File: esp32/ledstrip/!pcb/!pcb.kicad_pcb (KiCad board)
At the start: 2 copper layers, 100 x 100 mm, 11 parts, among them J1 Barrel_Jack_Switch, J2 Conn_01x03, U1 ESP32 MINI, U2 INMP441

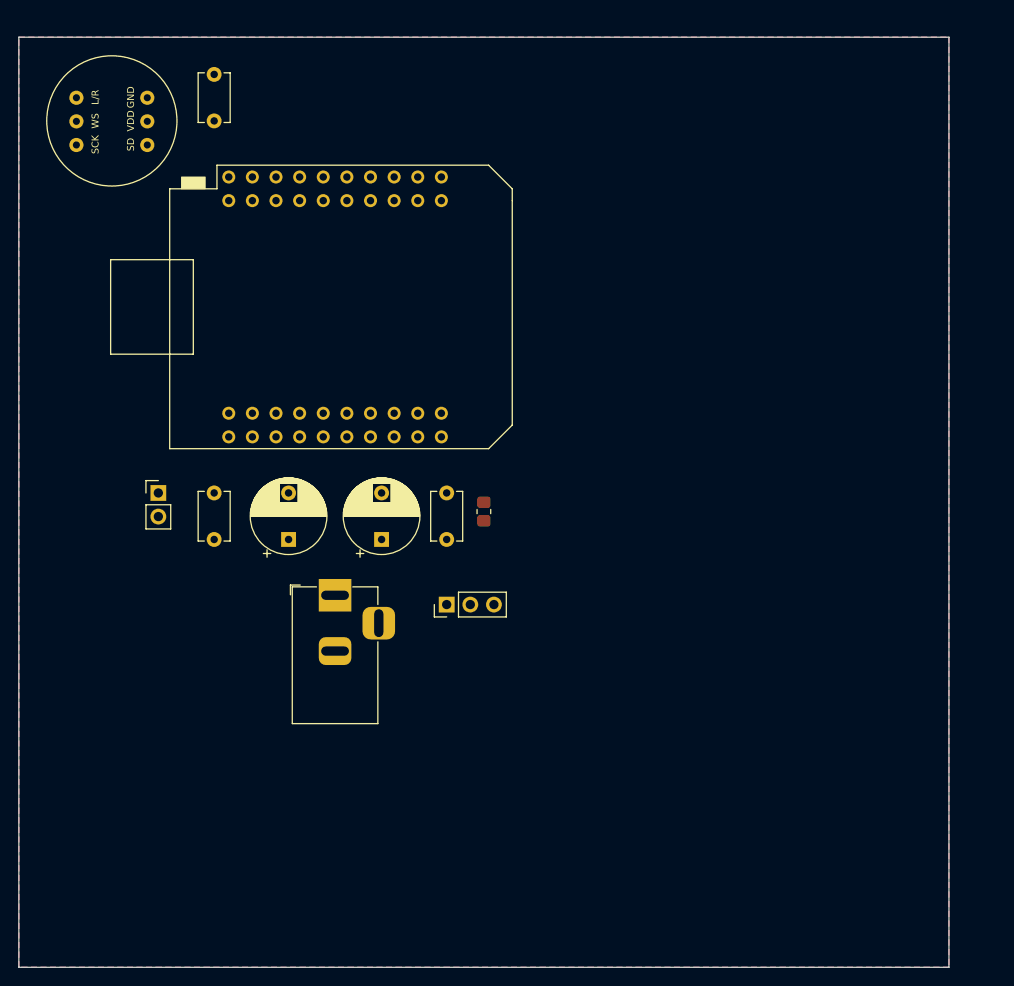
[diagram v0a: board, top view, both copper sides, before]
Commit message: ledstrip: Add SW
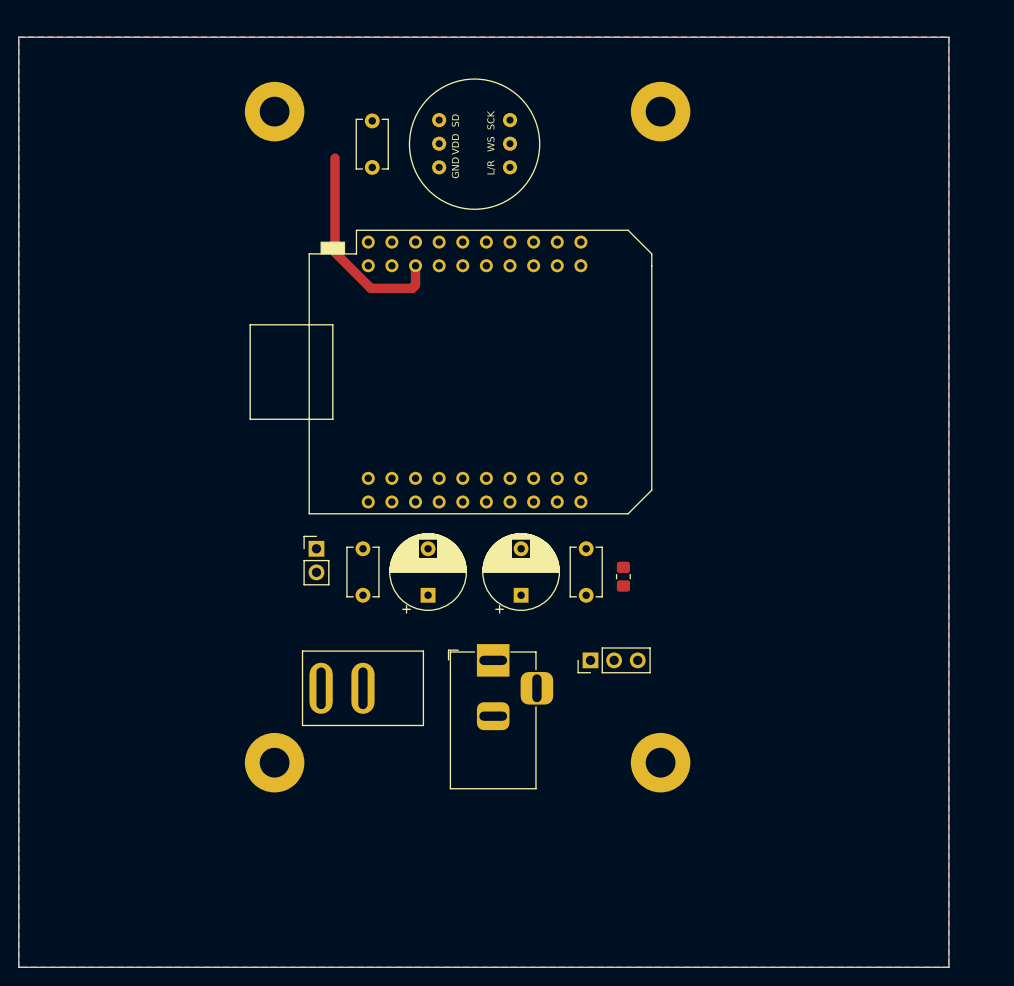
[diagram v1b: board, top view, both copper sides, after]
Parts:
- added H1: MountingHole_Pad, MountingHole:MountingHole_3.2mm_M3_Pad, F.Cu at (89.0, 53.0)
- added H2: MountingHole_Pad, MountingHole:MountingHole_3.2mm_M3_Pad, F.Cu at (47.5, 53.0)
- added H3: MountingHole_Pad, MountingHole:MountingHole_3.2mm_M3_Pad, F.Cu at (89.0, 123.0)
- added H4: MountingHole_Pad, MountingHole:MountingHole_3.2mm_M3_Pad, F.Cu at (47.5, 123.0)
- added SW1: SW_SPST, _my:sw, F.Cu at (57.0, 115.0)
- moved U2 39.1 mm to (69.0, 56.5), turned to 180 degrees
- moved J1 18.4 mm to (71.0, 112.0)
- moved JP1 18.0 mm to (52.0, 100.0)
- moved C3 17.1 mm to (57.0, 105.0)
- moved C5 17.0 mm to (58.0, 54.0), turned to 270 degrees
- moved J2 16.6 mm to (81.5, 112.0)
- moved R1 16.6 mm to (85.0, 103.0)
- moved U1 16.6 mm to (69.0, 81.0)
- moved C1 16.2 mm to (74.0, 105.0)
- moved C2 16.2 mm to (64.0, 105.0)
- moved C4 16.2 mm to (81.0, 105.0)
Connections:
- J1 pad 1: +5V -> Net-(J1-Pad1)
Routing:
- net +3V3: track 0.00 -> 22.6 mm

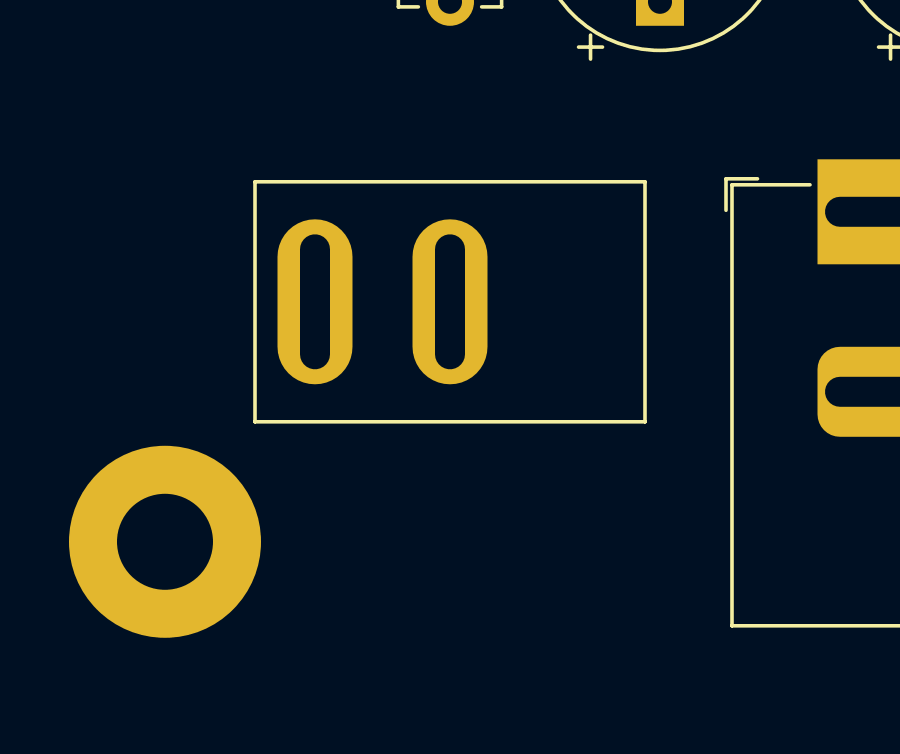
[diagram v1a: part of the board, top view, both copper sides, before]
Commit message: ledstrip: Adjust switch position
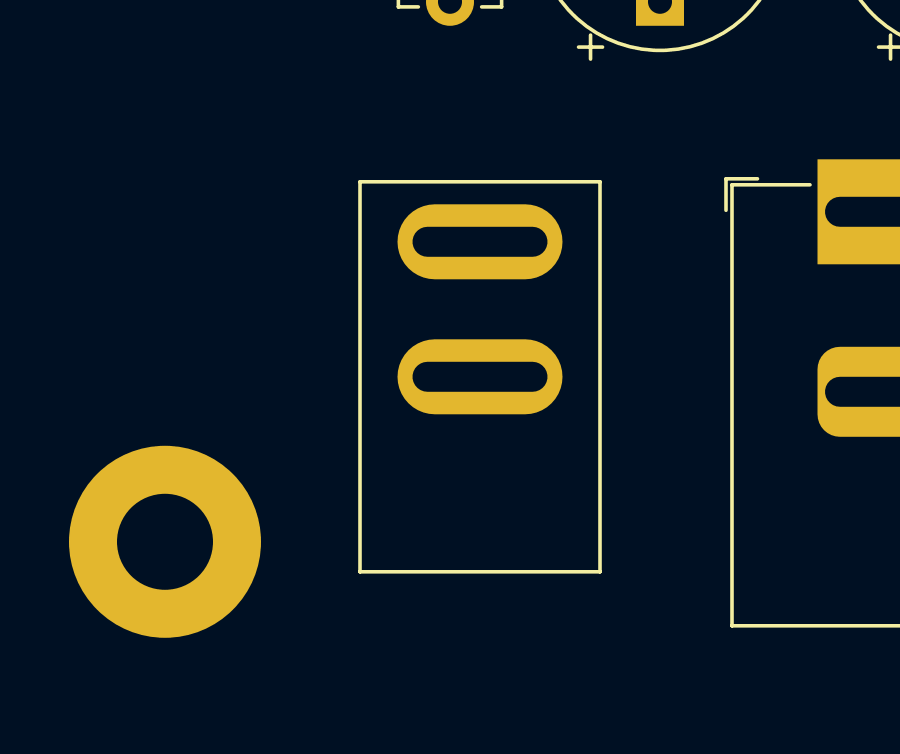
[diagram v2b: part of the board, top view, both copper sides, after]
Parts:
- moved SW1 2.69 mm to (58.0, 117.5), turned to 90 degrees

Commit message: ledstrip: Start routing
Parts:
- added G***: LOGO, _my:microusb, F.Cu at (52.5, 81.0)
- added G***: LOGO, _my:wifi, F.Cu at (87.0, 60.5)
- moved H3 3.16 mm to (86.0, 122.0)
- moved H1 3.00 mm to (86.0, 53.0)
- moved H4 2.69 mm to (50.0, 122.0)
- moved H2 2.50 mm to (50.0, 53.0)
- moved SW1 1.12 mm to (59.0, 118.0), turned to 270 degrees
- moved J1 1.00 mm to (71.0, 111.0)
- moved C5 0.50 mm to (58.0, 54.5)
- moved U2 0.50 mm to (69.0, 57.0)
- moved J2 0.46 mm to (81.0, 112.0)
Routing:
- net +5V: track 0.00 -> 50.8 mm
- net GND: track 0.00 -> 38.8 mm
- net Net-(J1-Pad1): track 0.00 -> 21.7 mm
- net Net-(JP1-Pad1): track 0.00 -> 17.4 mm
- net +3V3: track 22.6 -> 34.6 mm
- net STRIP: track 0.00 -> 10.9 mm
- net Net-(J2-Pad2): track 0.00 -> 8.64 mm
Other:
- board size 100 x 100 mm -> 44 x 77 mm
- board text added: "1000uF"
- board text added: "10uF"
- board text added: "330R"
- board text added: "3V3"
- board text added: "5V"
- board text added: "REMOVE BEFORE PROG"
- board text added: "https://github.com/tantecky/embedded"
- board text added: "v1.0"

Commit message: ledstrip: Routing is almost done
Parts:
- moved J2 2.00 mm to (81.0, 110.0)
- moved J1 1.00 mm to (70.0, 111.0)
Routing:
- net SD: track 0.00 -> 51.4 mm
- net SCK: track 0.00 -> 40.1 mm
- net WS: track 0.00 -> 36.5 mm
- net GND: track 38.8 -> 24.0 mm, vias 0 -> 22
- net +5V: track 50.8 -> 48.8 mm
- net Net-(J2-Pad2): track 8.64 -> 6.64 mm
- net Net-(J1-Pad1): track 21.7 -> 22.8 mm
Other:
- board text added: "-"

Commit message: ledstrip: Add JLCJLCJLC text
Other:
- board text added: "JLCJLCJLCJLC"
- board text added: "LEDstrip"

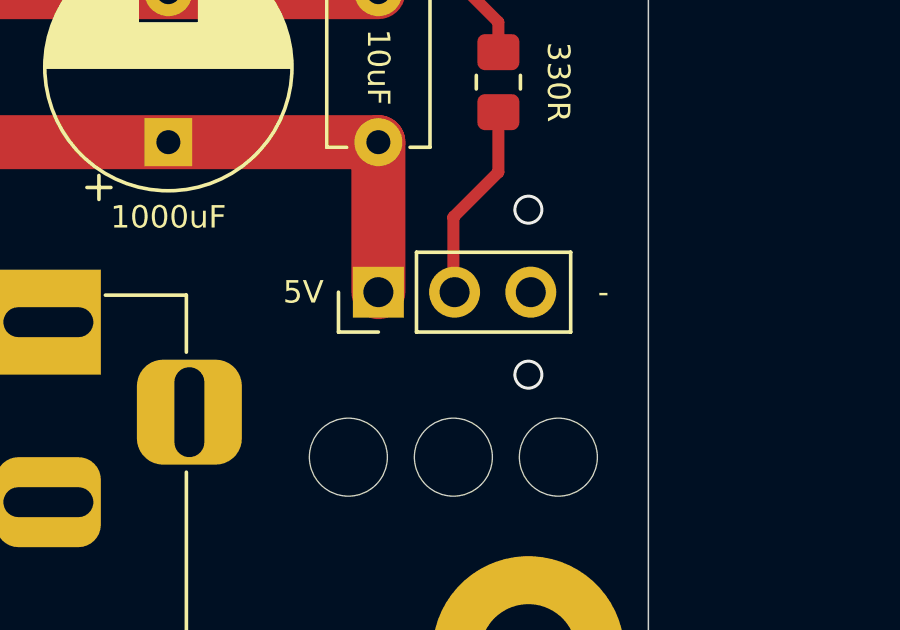
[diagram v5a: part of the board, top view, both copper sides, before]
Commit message: ledstrip: Ready for fab
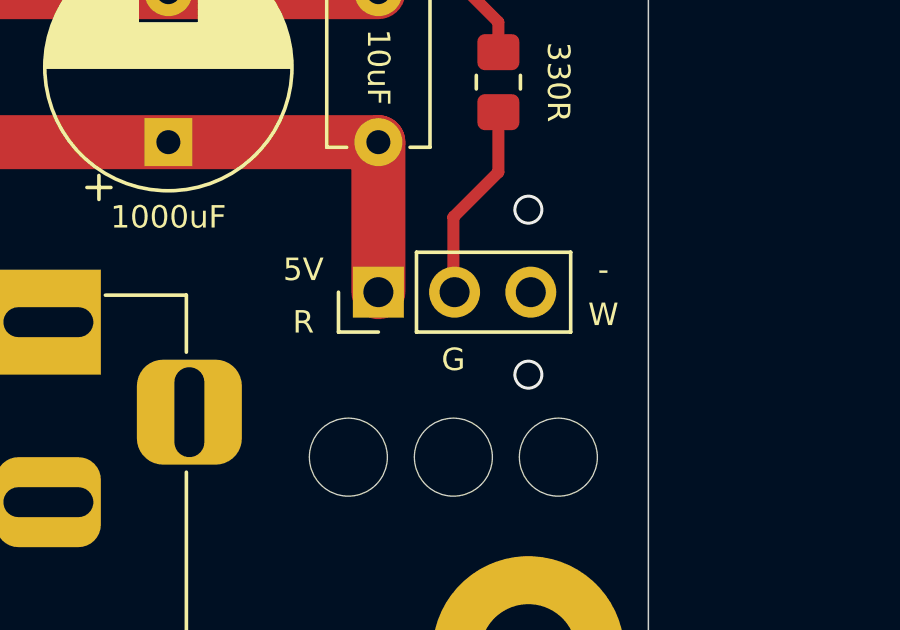
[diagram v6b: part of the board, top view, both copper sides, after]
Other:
- board text added: "G"
- board text added: "R"
- board text added: "W"
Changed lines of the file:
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@@
   (general
     (thickness 1.6)
-    (drawings 23)
+    (drawings 26)
     (tracks 73)
     (zones 0)
@@
       (net 1 GND))
   )
+  (gr_text G (at 83.5 112.25) (layer F.SilkS)
+    (effects (font (size 0.75 0.75) (thickness 0.15)))
+  )
+  (gr_text W (at 88.5 110.75) (layer F.SilkS)
+    (effects (font (size 0.75 0.75) (thickness 0.15)))
+  )
+  (gr_text R (at 78.5 111) (layer F.SilkS)
+    (effects (font (size 0.75 0.75) (thickness 0.15)))
+  )
   (gr_text JLCJLCJLCJLC (at 78 125) (layer B.SilkS)
     (effects (font (size 1 1) (thickness 0.15)) (justify mirror))
@@
     (effects (font (size 0.75 0.75) (thickness 0.15)))
   )
-  (gr_text - (at 88.5 110) (layer F.SilkS)
+  (gr_text - (at 88.5 109.25) (layer F.SilkS)
     (effects (font (size 0.75 0.75) (thickness 0.15)))
   )
@@
     (effects (font (size 0.75 0.75) (thickness 0.15)))
   )
-  (gr_text 5V (at 78.5 110) (layer F.SilkS)
+  (gr_text 5V (at 78.5 109.25) (layer F.SilkS)
     (effects (font (size 0.75 0.75) (thickness 0.15)))
   )

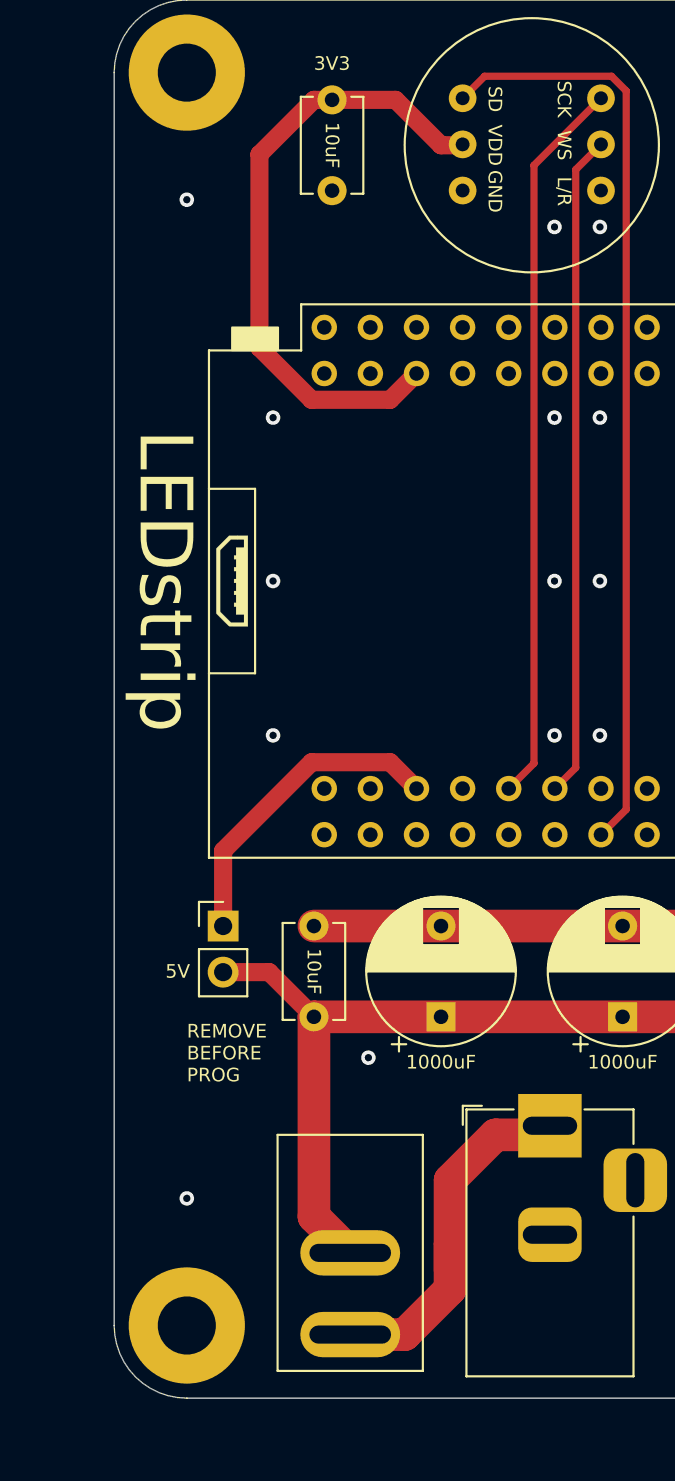
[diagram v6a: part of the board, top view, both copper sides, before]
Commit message: ledstrip: Reorient power switch
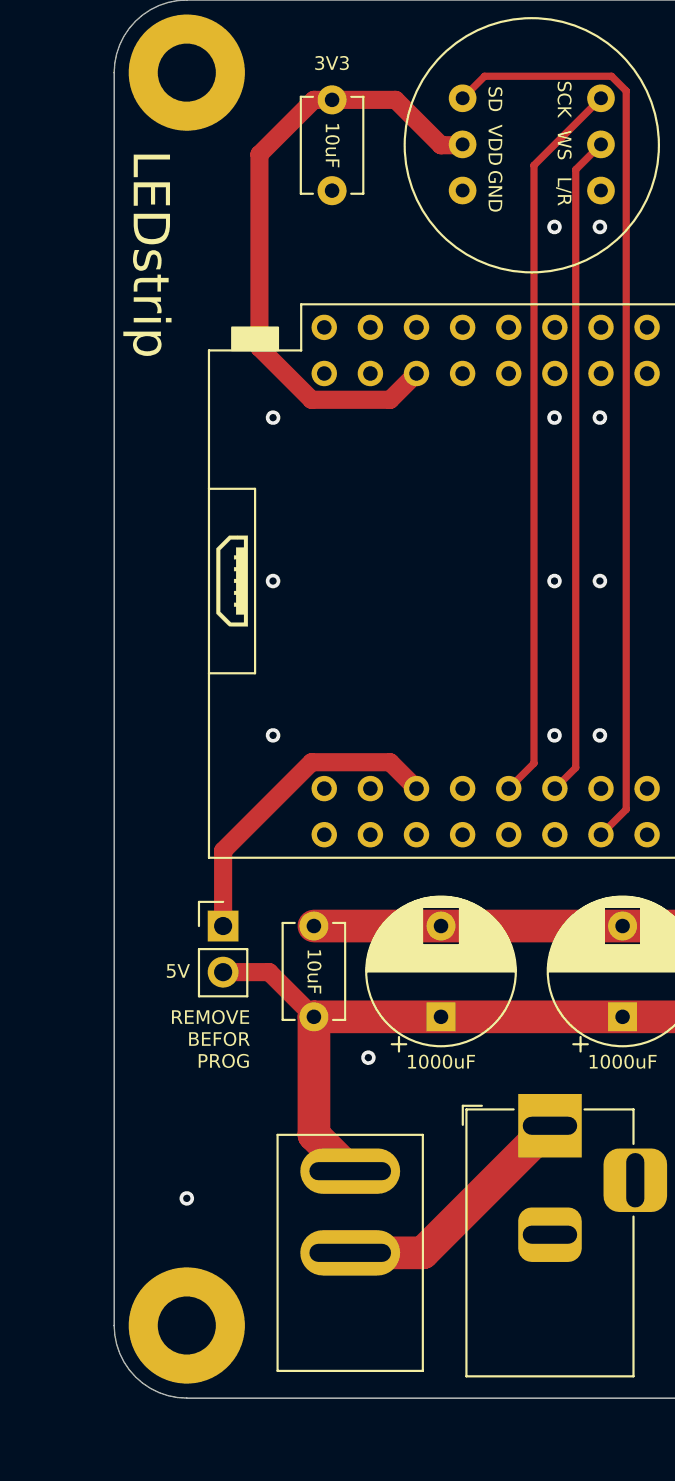
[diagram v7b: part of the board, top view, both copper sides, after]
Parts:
- turned SW1 to 90 degrees
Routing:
- net Net-(J1-Pad1): track 22.8 -> 14.6 mm
- net +5V: track 48.8 -> 44.3 mm
- net GND: vias 22 -> 21
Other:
- board text added: "REMOVE BEFOR PROG"
- board text removed: "REMOVE BEFORE PROG"

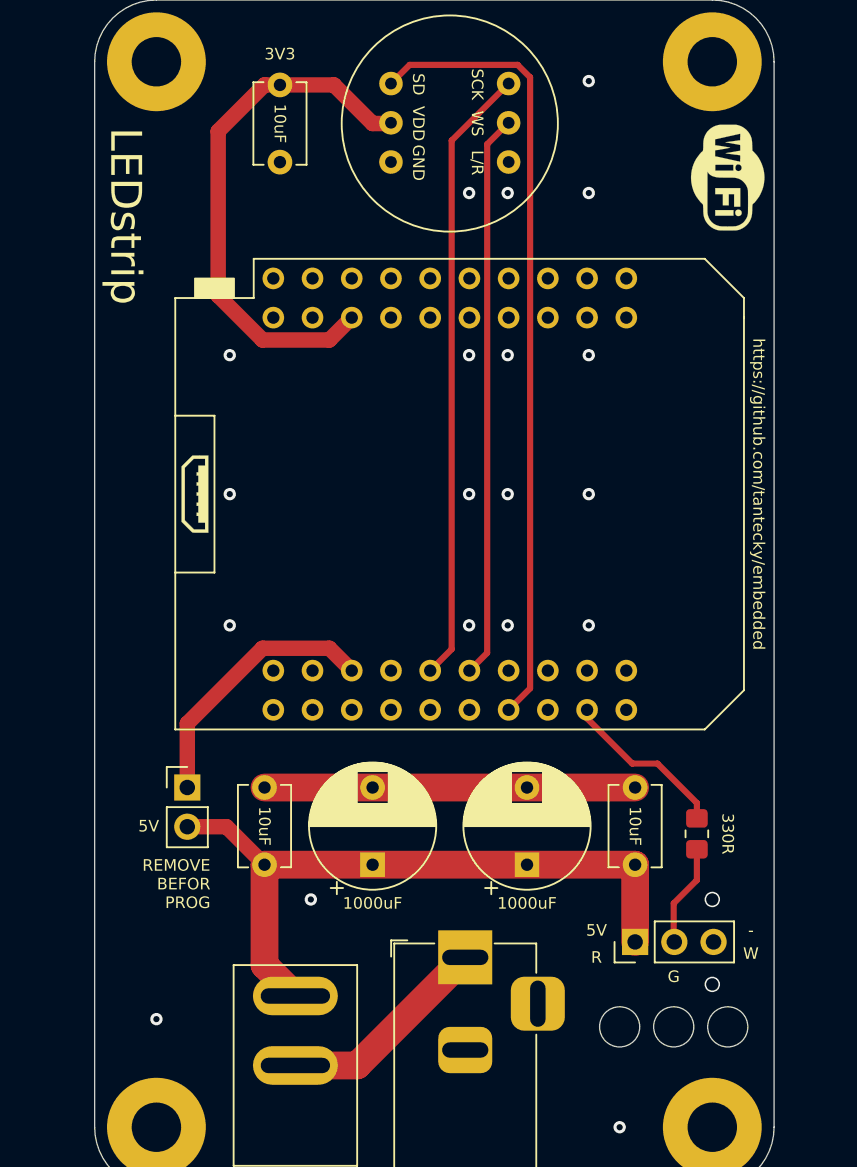
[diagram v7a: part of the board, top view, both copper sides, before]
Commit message: ledstrip: Adjust labels
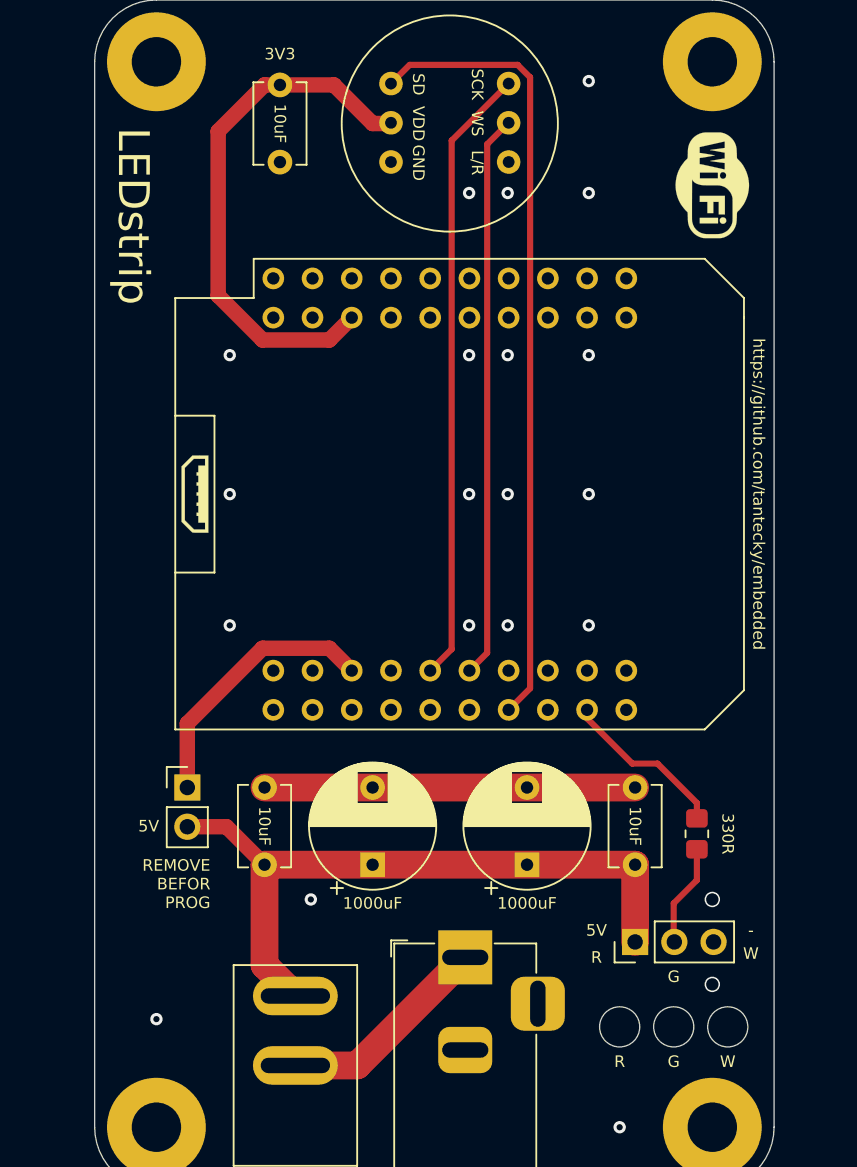
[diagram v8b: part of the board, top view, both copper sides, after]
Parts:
- moved G*** 1.12 mm to (86.0, 61.0)
